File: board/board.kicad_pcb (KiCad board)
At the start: 4 copper layers, 21 x 61 mm, 41 parts, among them J1 UART, J2 008_USB, J3 DebugEdge_02x05, J4 SPI_2x3, J5 ADC_2x3, J6 021_single_IO_UNIO, J7 SPI_2x3, J8 I2C_2x2, J9 UART_2x2, U1 W25Q16JVUXIQ, U2 RP2040, Y1 12MhZ

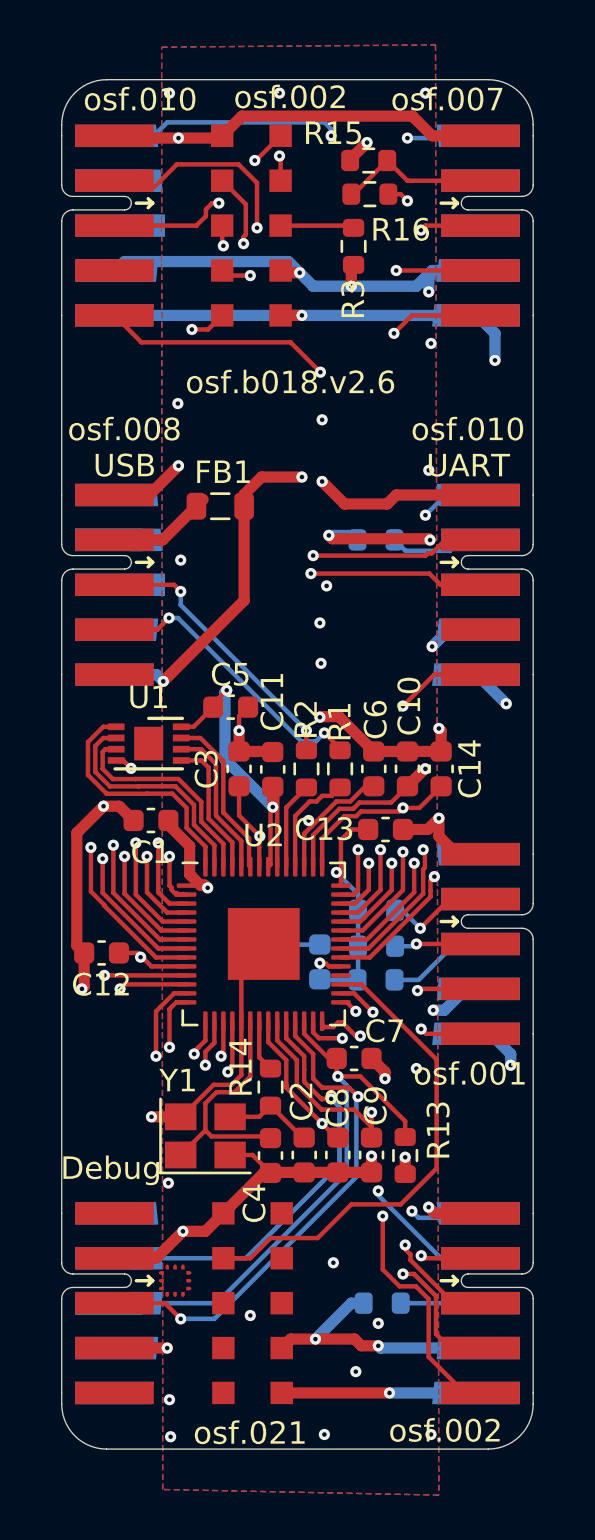
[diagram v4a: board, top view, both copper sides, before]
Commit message: updated I2C to fixed pinning
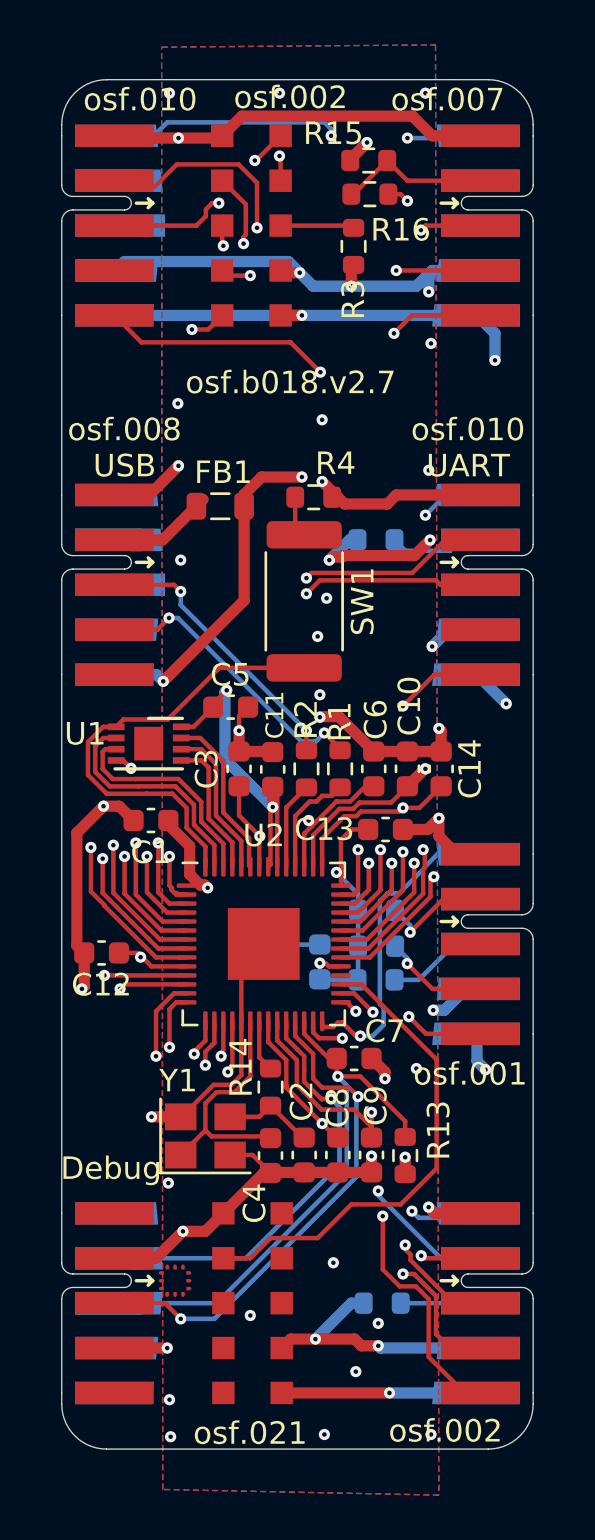
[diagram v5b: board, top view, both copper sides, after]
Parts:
- added R4: 1k, Resistor_SMD:R_0603_1608Metric, F.Cu at (151.2, 60.6)
- added SW1: PTS636 SK25J SMTR LFS, Resistor_SMD:R_2512_6332Metric, F.Cu at (150.8, 65.2)
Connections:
- J8 pad 3: /I2C1_SCL -> unconnected-(J8-N/C-Pad3)
- J8 pad 4: /GPIO16 -> /I2C1_SCL
- J8 pad 5: /GPIO17 -> /GPIO16
- J8 pad 6: (no net) -> /GPIO17
- J8 pad 7: (no net) -> unconnected-(J8-status-Pad7)
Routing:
- net /rp2040/QPI_SS: track 11.0 -> 20.4 mm
- net /GPIO17: track 7.80 -> 14.4 mm, vias 2 -> 1
- net Net-(R4-Pad2): track 0.00 -> 1.84 mm
- net +5V: track 107.4 -> 106.3 mm
- net /UART1_RX: track 32.9 -> 32.2 mm
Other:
- board text added: "osf.b018.v2.7"
- board text removed: "osf.b018.v2.6"
